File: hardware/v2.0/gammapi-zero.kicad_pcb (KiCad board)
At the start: 4 copper layers, 65 x 30 mm, 210 parts, among them IC1 IS42S16160J-6BLI, IC3 LM4040AIM3-2.0_NOPB, IC4 LTC2622IMS8#PBF, IC5 LTC6409IUDB#TRPBF, IC6 ADS6122IRHBT, J1 Conn_02x20_Counter_Clockwise, J2 GPDI_C_1.3, J3 USB_C_Receptacle_USB2.0_14P, J4 USB_C_Receptacle_USB2.0_14P, J5 USB_C_Receptacle_USB2.0_14P, J6 Micro_SD_Card_Det2, J7 RSP-122811-01, J8 BM04B-ACHSS-A-GAN-TF_LF__SN_, SW1 SW_Push, SW2 SW_Push, U1 ECP5U-25F-CABGA256, U10 TPD2EUSB30A, U12 W25Q128JVS, U2 LTC3407AEDD-2_PBF, U3 TLV62569DBV, U6 PCA9306DC1, U7 TPD2EUSB30A, U8 TPD2EUSB30A, U9 FT231XQ, Y1 SG-8018CG 50.000000MHz, Y2 SG-8018CG 50.000000MHz

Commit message: Minor changes
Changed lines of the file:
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@@
 			(at 0 -1.5 90)
 			(layer "F.SilkS")
+			(hide yes)
 			(effects
 				(font
@@
 			(at 0 -1.5 90)
 			(layer "F.SilkS")
+			(hide yes)
 			(effects
 				(font
@@
 			(at 0 1.5 270)
 			(layer "B.SilkS")
+			(hide yes)
 			(effects
 				(font

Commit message: Update gammapi-zero.kicad_pcb
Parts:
- IC1: value IS42S16160J-6BLI -> IS42S16160J-6BLI-TR
- J8: value BM04B-ACHSS-A-GAN-TF_LF__SN_ -> BM04B-ACHSS-A-GAN-TF(LF)(SN)
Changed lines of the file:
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@@
 			)
 		)
+		(property "LCSC Part #" "C1542915"
+			(at 0 0 90)
+			(unlocked yes)
+			(layer "F.Fab")
+			(hide yes)
+			(effects
+				(font
+					(size 1 1)
+					(thickness 0.15)
+				)
+			)
+		)
 		(sheetname "/ADC/")
 		(sheetfile "adc.kicad_sch")
@@
 			(at 0 0 90)
 			(layer "F.SilkS")
+			(hide yes)
 			(effects
 				(font
@@
 			)
 		)
+		(property "LCSC Part #" "C689302"
+			(at 0 0 90)
+			(unlocked yes)
+			(layer "F.Fab")
+			(hide yes)
+			(effects
+				(font
+					(size 1 1)
+					(thickness 0.15)
+				)
+			)
+		)
 		(sheetname "/ADC/")
 		(sheetfile "adc.kicad_sch")
@@
 			)
 		)
+		(property "LCSC Part #" "C7429437"
+			(at 0 0 0)
+			(unlocked yes)
+			(layer "F.Fab")
+			(hide yes)
+			(effects
+				(font
+					(size 1 1)
+					(thickness 0.15)
+				)
+			)
+		)
 		(sheetname "/")
 		(sheetfile "gammapi-zero.kicad_sch")
@@
 			)
 		)
+		(property "LCSC Part #" "C7429437"
+			(at 0 0 0)
+			(unlocked yes)
+			(layer "F.Fab")
+			(hide yes)
+			(effects
+				(font
+					(size 1 1)
+					(thickness 0.15)
+				)
+			)
+		)
 		(sheetname "/")
 		(sheetfile "gammapi-zero.kicad_sch")
@@
 			)
 		)
+		(property "LCSC Part #" "C2938932"
+			(at 0 0 270)
+			(unlocked yes)
+			(layer "F.Fab")
+			(hide yes)
+			(effects
+				(font
+					(size 1 1)
+					(thickness 0.15)
+				)
+			)
+		)
 		(sheetname "/ADC/")
 		(sheetfile "adc.kicad_sch")
@@
 			)
 		)
-		(property "LCSC Part #" "C25744"
+		(property "LCSC Part #" "C25741"
 			(at 0 0 270)
 			(unlocked yes)
@@
 			)
 		)
+		(property "LCSC Part #" "C684618"
+			(at 0 0 0)
+			(unlocked yes)
+			(layer "F.Fab")
+			(hide yes)
+			(effects
+				(font
+					(size 1 1)
+					(thickness 0.15)
+				)
+			)
+		)
 		(sheetname "/Power/")
 		(sheetfile "power.kicad_sch")
@@
 			)
 		)
+		(property "LCSC Part #" "C1521614"
+			(at 0 0 270)
+			(unlocked yes)
+			(layer "F.Fab")
+			(hide yes)
+			(effects
+				(font
+					(size 1 1)
+					(thickness 0.15)
+				)
+			)
+		)
 		(sheetname "/")
 		(sheetfile "gammapi-zero.kicad_sch")
@@
 			)
 		)
+		(property "LCSC Part #" "C7429437"
+			(at 0 0 0)
+			(unlocked yes)
+			(layer "F.Fab")
+			(hide yes)
+			(effects
+				(font
+					(size 1 1)
+					(thickness 0.15)
+				)
+			)
+		)
 		(sheetname "/")
 		(sheetfile "gammapi-zero.kicad_sch")
@@
 			)
 		)
+		(property "LCSC Part #" "C7429437"
+			(at 0 0 0)
+			(unlocked yes)
+			(layer "F.Fab")
+			(hide yes)
+			(effects
+				(font
+					(size 1 1)
+					(thickness 0.15)
+				)
+			)
+		)
 		(sheetname "/")
 		(sheetfile "gammapi-zero.kicad_sch")
@@
 			)
 		)
-		(property "Value" "IS42S16160J-6BLI"
+		(property "Value" "IS42S16160J-6BLI-TR"
 			(at 0 0 90)
 			(layer "F.SilkS")
@@
 			)
 		)
+		(property "LCSC Part #" "C2063680"
+			(at 0 0 270)
+			(unlocked yes)
+			(layer "F.Fab")
+			(hide yes)
+			(effects
+				(font
+					(size 1 1)
+					(thickness 0.15)
+				)
+			)
+		)
 		(sheetname "/SDRAM/")
 		(sheetfile "sdram.kicad_sch")
@@
 			)
 		)
+		(property "LCSC Part #" "C7429437"
+			(at 0 0 0)
+			(unlocked yes)
+			(layer "F.Fab")
+			(hide yes)
+			(effects
+				(font
+					(size 1 1)
+					(thickness 0.15)
+				)
+			)
+		)
 		(sheetname "/")
 		(sheetfile "gammapi-zero.kicad_sch")
@@
 			)
 		)
-		(property "LCSC Part #" "C77571"
+		(property "LCSC Part #" "C1532"
 			(at 0 0 0)
 			(unlocked yes)
@@
 			)
 		)
-		(property "LCSC Part #" "C77571"
+		(property "LCSC Part #" "C1532"
 			(at 0 0 180)
 			(unlocked yes)
@@
 			)
 		)
-		(property "LCSC Part #" "C77571"
+		(property "LCSC Part #" "C1532"
 			(at 0 0 180)
 			(unlocked yes)
@@
 			)
 		)
-		(property "LCSC Part #" "C77571"
+		(property "LCSC Part #" "C1532"
 			(at 0 0 180)
 			(unlocked yes)
@@
 			)
 		)
-		(property "LCSC Part #" "C77571"
+		(property "LCSC Part #" "C1532"
 			(at 0 0 90)
 			(unlocked yes)
@@
 			)
 		)
+		(property "LCSC Part #" "C580579"
+			(at 0 0 270)
+			(unlocked yes)
+			(layer "B.Fab")
+			(hide yes)
+			(effects
+				(font
+					(size 1 1)
+					(thickness 0.15)
+				)
+				(justify mirror)
+			)
+		)
 		(sheetname "/DAC/")
 		(sheetfile "dac.kicad_sch")
@@
 			)
 		)
+		(property "LCSC Part #" "C2156507"
+			(at 0 0 0)
+			(unlocked yes)
+			(layer "B.Fab")
+			(hide yes)
+			(effects
+				(font
+					(size 1 1)
+					(thickness 0.15)
+				)
+				(justify mirror)
+			)
+		)
 		(sheetname "/DAC/")
 		(sheetfile "dac.kicad_sch")
@@
 			)
 		)
-		(property "Value" "BM04B-ACHSS-A-GAN-TF_LF__SN_"
+		(property "Value" "BM04B-ACHSS-A-GAN-TF(LF)(SN)"
 			(at 0.15 0 180)
 			(layer "B.SilkS")
@@
 			)
 		)
+		(property "LCSC Part #" "C5246838"
+			(at 0 0 0)
+			(unlocked yes)
+			(layer "B.Fab")
+			(hide yes)
+			(effects
+				(font
+					(size 1 1)
+					(thickness 0.15)
+				)
+				(justify mirror)
+			)
+		)
 		(sheetname "/DAC/")
 		(sheetfile "dac.kicad_sch")
@@
 			)
 		)
-		(property "LCSC Part #" "C77571"
+		(property "LCSC Part #" "C1532"
 			(at 0 0 180)
 			(unlocked yes)
@@
 			)
 		)
-		(property "LCSC Part #" "C77571"
+		(property "LCSC Part #" "C1532"
 			(at 0 0 180)
 			(unlocked yes)

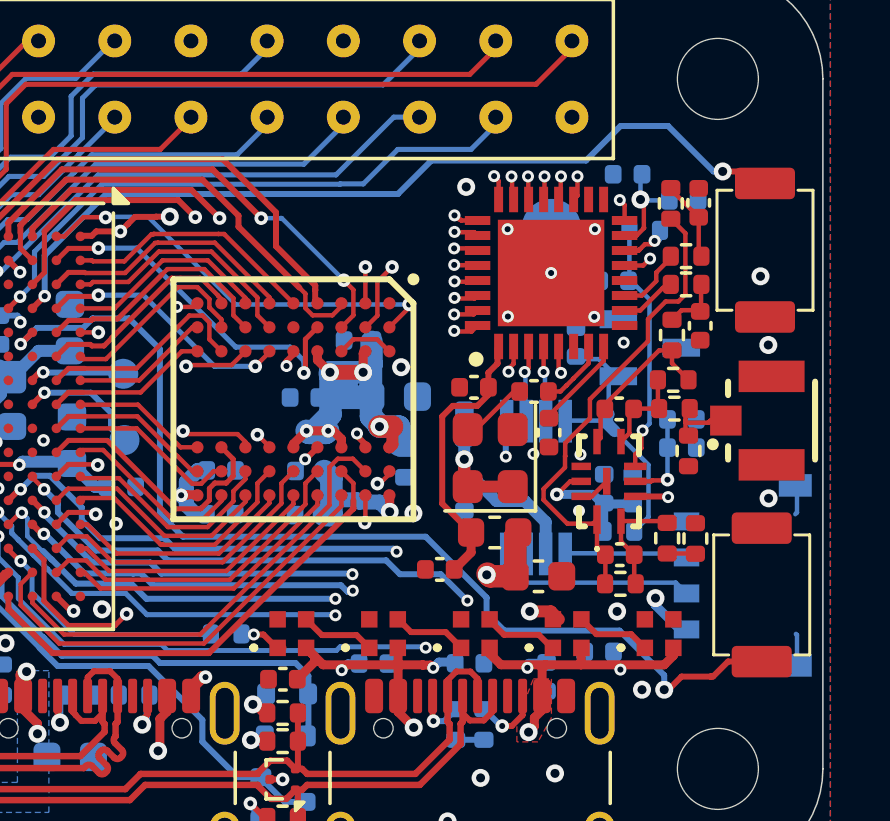
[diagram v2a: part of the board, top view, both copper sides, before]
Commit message: ADA4932-1 amplifier
ADA4932-1 amplifier replaced LTC6409
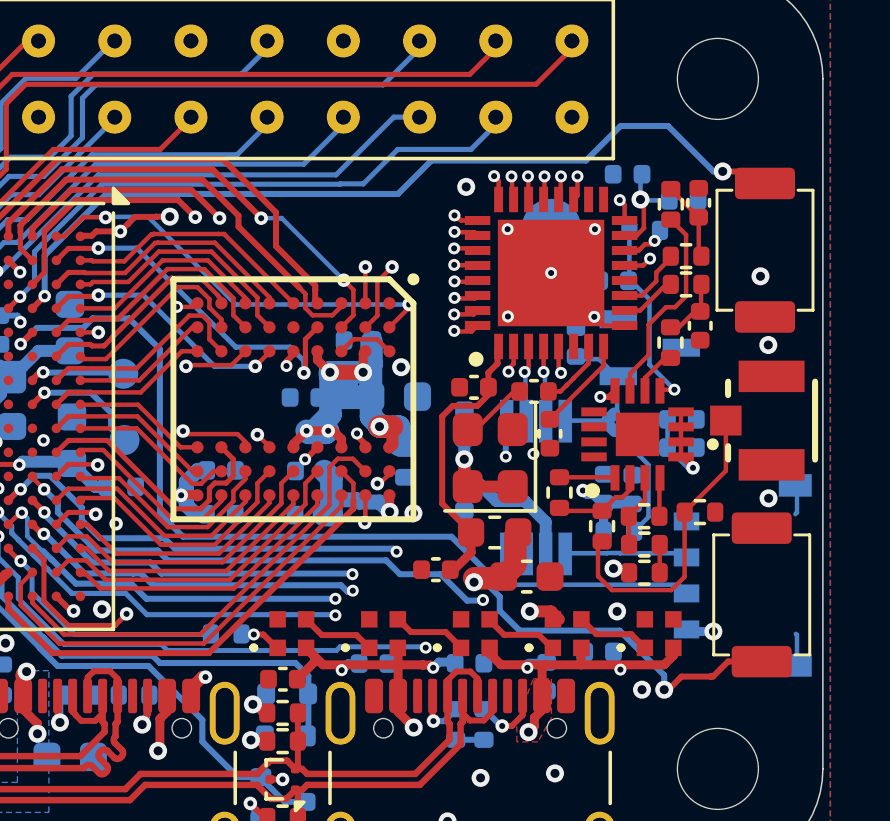
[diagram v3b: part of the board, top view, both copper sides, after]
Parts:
- removed C78, C84: 1p3, Capacitor_SMD:C_0402_1005Metric
- removed IC5: LTC6409IUDB#TRPBF, LTC6409IUDB#TRPBF:LTC6409IUDBTRPBF
- removed R62: 28R7, Resistor_SMD:R_0402_1005Metric
- added IC2: ADA4932-1YCPZ-R7, ADA4932-1YCPZ-R7:QFN50P300X300X80-17N-D, F.Cu at (174.6, 105.3)
- added R56: 499R, Resistor_SMD:R_0402_1005Metric, F.Cu at (174.8, 109.0)
- R52: value 150R -> 499R
- R57: value 150R -> 511R
- R59: value 66R5 -> 511R
- R60: value 150R -> 25R5
- R61: value 150R -> 53R6
- moved R52 5.43 mm to (173.4, 108.4), turned to -90 degrees
- moved R57 4.74 mm to (172.0, 107.3), turned to 90 degrees
- moved R59 2.63 mm to (174.8, 108.1), turned to 180 degrees
- moved R61 1.39 mm to (176.7, 107.9), turned to 180 degrees
- moved R60 0.88 mm to (174.8, 110.0)
- moved C62 0.39 mm to (170.9, 110.1)
- moved R51 0.25 mm to (175.7, 102.3)
- moved C65 0.13 mm to (167.8, 109.9)
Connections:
- R5 pad 1: Net-(IC5--OUT) -> Net-(IC2--OUT)
- R51 pad 1: Net-(IC5-+OUT) -> Net-(IC2-+OUT)
- R52 pad 1: Net-(IC5-+OUT) -> Net-(IC2-+IN)
- R52 pad 2: Net-(IC5--IN) -> Net-(J7-Pad1)
- R57 pad 1: Net-(IC5--IN) -> Net-(IC2-+IN)
- R57 pad 2: Net-(J7-Pad1) -> Net-(IC2--FB)
- R59 pad 1: Net-(J7-Pad1) -> Net-(IC2-+FB)
- R59 pad 2: GND -> Net-(IC2--IN)
- R60 pad 1: Net-(IC5--OUT) -> GND
- R60 pad 2: Net-(IC5-+IN) -> Net-(R56-Pad1)
- R61 pad 1: Net-(IC5-+IN) -> GND
- R61 pad 2: Net-(R61-Pad2) -> Net-(J7-Pad1)
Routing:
- net Net-(IC5--OUT): track 16.2 -> 0.00 mm
- net Net-(J7-Pad1): track 2.27 -> 10.3 mm
- net Net-(IC2--OUT): track 0.00 -> 6.87 mm
- net Net-(IC5-+OUT): track 5.48 -> 0.00 mm
- net Net-(IC5-+IN): track 3.86 -> 0.00 mm
- net Net-(IC2-+IN): track 0.00 -> 3.06 mm
- net Net-(IC5--IN): track 3.06 -> 0.00 mm
- net Net-(IC2--IN): track 0.00 -> 2.45 mm
- net /ADC/VOCM: track 8.41 -> 6.50 mm
- net Net-(IC2--FB): track 0.00 -> 1.86 mm
- net Net-(IC2-+OUT): track 0.00 -> 1.56 mm
- net +3V3: track 142.5 -> 141.2 mm
- net Net-(IC2-+FB): track 0.00 -> 1.29 mm
- net Net-(R61-Pad2): track 0.94 -> 0.00 mm
- net Net-(R56-Pad1): track 0.00 -> 0.94 mm
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
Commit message: TLV62569DBVR Voltage Regulator
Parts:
- removed R53, R54: 4M7, Resistor_SMD:R_0402_1005Metric
- removed R55: 100k, Resistor_SMD:R_0402_1005Metric
- added U3: TLV62569DBV, Package_TO_SOT_SMD:SOT-23-5, F.Cu at (134.1, 103.2)
- C12: value 5n6 -> 22u; footprint Capacitor_SMD:C_0402_1005Metric -> Capacitor_SMD:C_0603_1608Metric; moved to B.Cu
- C18: value 2n7 -> 22u; footprint Capacitor_SMD:C_0402_1005Metric -> Capacitor_SMD:C_0603_1608Metric
- C56, C57: value 22p -> 100p
- C58: value 6.8p -> 100p
- J8: value BM04B-ACHSS-A-GAN-TF(LF)(SN) -> GT-A1201WRS-104B1101
- R10: value 453k -> 15k
- R11: value 100k -> 3.3k
- R6: value 255k -> 15k
- R7: value 301k -> 18k
- R8: value 887k -> 15k
- R9: value 280k -> 4.7k
- U2: value LTC3407AEDD-2_PBF -> TLV62569DBV; footprint LTC3407AEDD-2_PBF:DFN-10_DD -> Package_TO_SOT_SMD:SOT-23-5
- moved C11 7.26 mm to (131.3, 104.4), turned to -90 degrees
- moved C12 3.75 mm to (130.9, 104.7), turned to 0 degrees
- moved U2 3.26 mm to (129.9, 101.2)
- moved R9 2.71 mm to (131.9, 102.8), turned to -90 degrees
- moved C18 1.75 mm to (134.0, 100.8), turned to 0 degrees
- moved C33 1.28 mm to (128.3, 98.0), turned to 90 degrees
- moved C56 0.98 mm to (130.7, 102.5)
- moved C57 0.67 mm to (132.9, 102.8)
- moved C13 0.52 mm to (129.1, 105.8)
- moved R8 0.31 mm to (133.9, 102.8)
- moved C20 0.30 mm to (134.8, 102.8)
- renumbered U3 to U4
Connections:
- C12 pad 1: GND -> +1V1
- C12 pad 2: Net-(U2-RUN/SS1) -> GND
- C18 pad 1: Net-(U2-RUN/SS2) -> +5V
- C56 pad 2: /Power/VFB1 -> Net-(U2-FB)
- C57 pad 2: /Power/VFB2 -> Net-(U3-FB)
- L1 pad 1: /Power/SW1 -> Net-(U2-SW)
- L2 pad 1: /Power/SW2 -> Net-(U3-SW)
- R6 pad 2: /Power/VFB1 -> Net-(U2-FB)
- R7 pad 1: /Power/VFB1 -> Net-(U2-FB)
- R8 pad 2: /Power/VFB2 -> Net-(U3-FB)
- R9 pad 1: /Power/VFB2 -> Net-(U3-FB)
- U2 pad 1: /Power/VFB1 -> +5V
- U2 pad 2: Net-(U2-RUN/SS1) -> GND
- U2 pad 3: +5V -> Net-(U2-SW)
- U2 pad 4: /Power/SW1 -> +5V
- U2 pad 5: GND -> Net-(U2-FB)
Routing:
- net Net-(U2-FB): track 0.00 -> 4.10 mm, vias 0 -> 1
- net Net-(U3-FB): track 0.00 -> 4.03 mm, vias 0 -> 1
- net Net-(U2-RUN/SS1): track 3.68 -> 0.00 mm
- net Net-(U2-RUN/SS2): track 3.65 -> 0.00 mm
- net /Power/VFB1: track 3.33 -> 0.00 mm, vias 1 -> 0
- net /Power/VFB2: track 3.32 -> 0.00 mm, vias 1 -> 0
- net Net-(U2-SW): track 0.00 -> 3.21 mm, vias 0 -> 1
- net Net-(U2-~{POR}): track 2.97 -> 0.00 mm
- net /Power/SW2: track 2.60 -> 0.00 mm, vias 1 -> 0
- net /Power/SW1: track 2.12 -> 0.00 mm, vias 1 -> 0
- net +2V5: track 13.7 -> 11.7 mm
- net Net-(U3-SW): track 0.00 -> 1.74 mm, vias 0 -> 1
- net +5V: track 219.8 -> 220.6 mm, vias 20 -> 19
- removed copper zone on F.Cu, net +2V5
